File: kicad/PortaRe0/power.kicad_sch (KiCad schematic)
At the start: 37 parts, among them SW1 SW_START, SW2 KillSW, U1 BQ25895RTWR, U2 TPS61023DRLR, U3 AP2112K-3.3TRG1

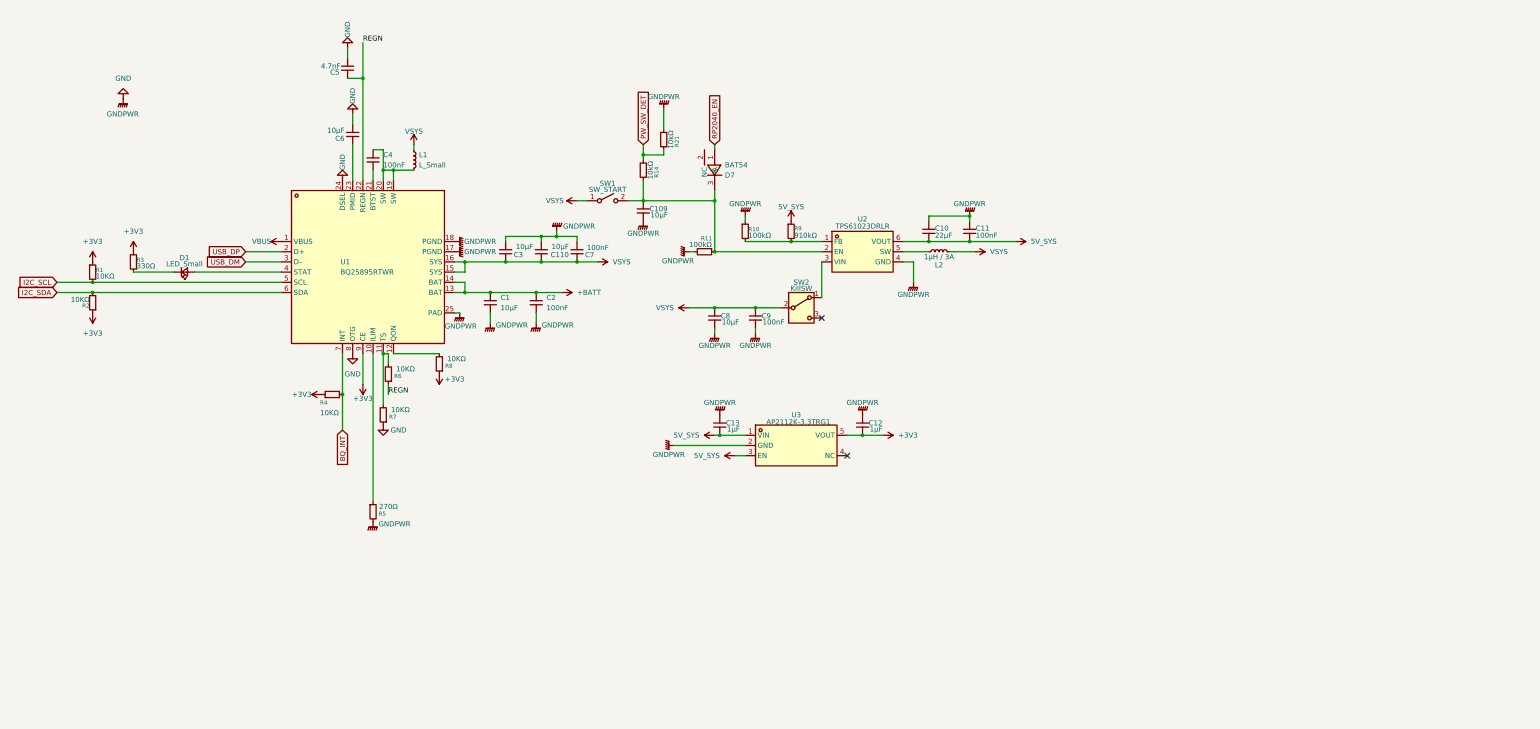
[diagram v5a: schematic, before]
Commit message: Docs: session18終了処理・PROGRESS/index更新・connectorsシート設計方針確定
- J_HDMI_CTRL: 24pin FPC 0.5mm (C2856805) ライブラリ取得・配置方針確定
- SBC接続: サブ基板→FPCに変更・スティフナーにMicro HDMIオス+USB-Cオス直付け方針
- connectors.kicad_sch 追加

Co-Authored-By: Claude Sonnet 4.6 <noreply@anthropic.com>
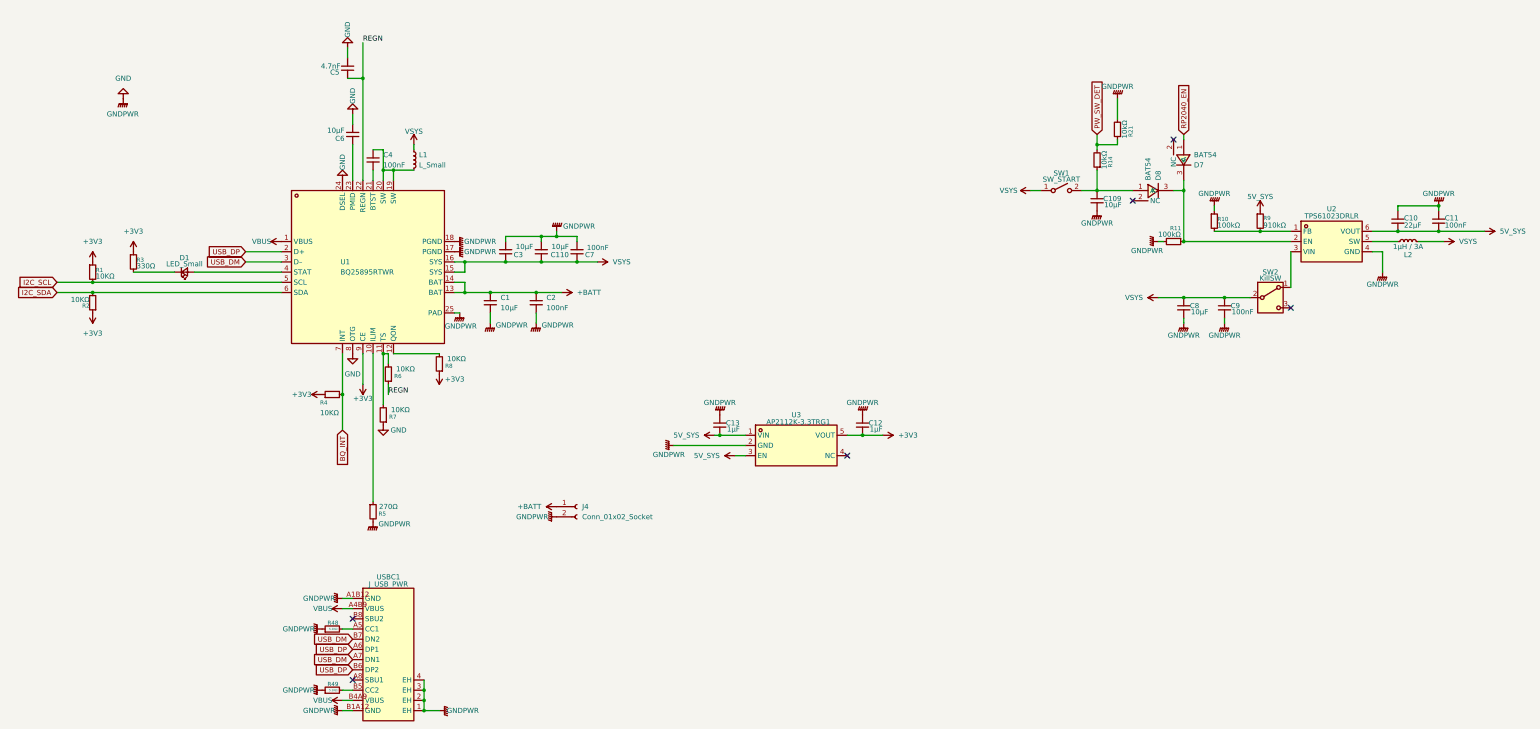
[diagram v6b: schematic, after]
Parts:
- added D8: BAT54, PortaRe0:SOT-23-3_L2.9-W1.4-P1.90-LS2.6-BR, symbol PortaRe0:BAT54_C466635
- added J4: Conn_01x02_Socket, symbol Connector:Conn_01x02_Socket
- added R48, R49: 5.1KΩ, symbol Device:R_Small
- added USBC1: J_USB_PWR, PortaRe0:USB-C_SMD-TYPE-C-31-M-12_1, symbol PortaRe0:TYPE-C-31-M-12
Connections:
- net +BATT: now also J4.1 (Pin_1)
- net GND: now also J4.2 (Pin_2), R48.1, R49.1, USBC1.1 (EH), USBC1.2 (EH), USBC1.3 (EH), USBC1.4 (EH), USBC1.A1B12 (GND), USBC1.B1A12 (GND)
- net USB_DM: now also USBC1.A7 (DN1), USBC1.B7 (DN2)
- net USB_DP: now also USBC1.A6 (DP1), USBC1.B6 (DP2)
- net VBUS: now also USBC1.A4B9 (VBUS), USBC1.B4A9 (VBUS)
- net at D7.3 (K), R11.1, U2.2 (EN): now also D8.3 (K); no longer C109.1, R14.1, SW1.2 (B)
- new net: R48.2, USBC1.A5 (CC1)
- new net: R49.2, USBC1.B5 (CC2)
- new net: C109.1, D8.1 (A), R14.1, SW1.2 (B)
- no-connect marks 2 -> 6
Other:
- moved on the sheet: C10, C109, C11, C8, C9, D7, L2, R10, R11, R14, R21, R9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

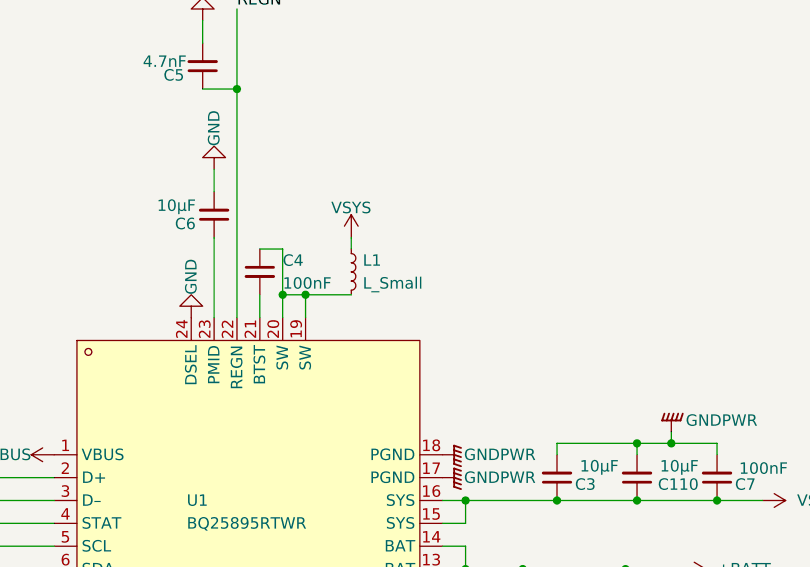
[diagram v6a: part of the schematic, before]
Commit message: KiCad/Docs: powerシートL1値2.2μH更新・README全面更新
- power.kicad_sch: L1インダクタ値を2.2μHに更新（BQ25895 TI例参照）
- README: バッテリー型番/容量修正・全シート完成状態に更新・部品C番号一覧追記

Co-Authored-By: Claude Sonnet 4.6 <noreply@anthropic.com>
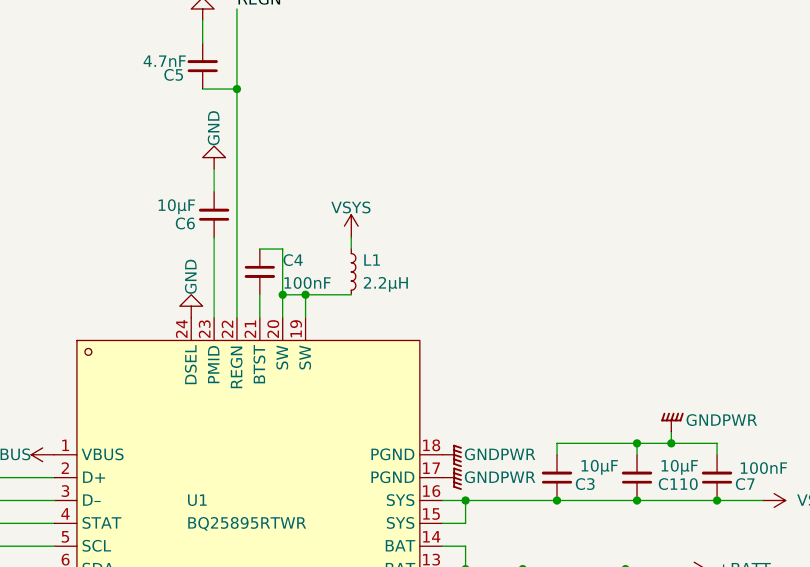
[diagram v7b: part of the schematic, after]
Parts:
- L1: value L_Small -> 2.2μH
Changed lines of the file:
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@@
 			)
 		)
-		(property "Value" "L_Small"
+		(property "Value" "2.2μH"
 			(at 113.03 52.0699 0)
 			(effects

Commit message: Docs/KiCad: session24終了処理・チェックシート作成・回路修正
- Claude/checklists/ 新規作成（IC設計レビュー用 01〜10）
- BQ25895修正: C5(4.7nF→4.7µF) / CE(3V3→GND) / QON(GND→NC)
- TPS61023修正: R_TOP(910kΩ→750kΩ, 5.1V) / SW2をVSYS直列に変更 / usb_hub SW4削除
- AP2112K: バイパスキャップ1µF→10µF
- PROGRESS.md・index.md更新

Co-Authored-By: Claude Sonnet 4.6 <noreply@anthropic.com>
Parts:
- removed R8: 10KΩ, symbol Device:R_Small
- added C113: 10μF, symbol Device:C_Small
- added C114: 100nF, symbol Device:C_Small
- C12, C13: value 1µF -> 10µF
- C5: value 4.7nF -> 4.7μF
- R9: value 910kΩ -> 750kΩ
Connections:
- net +3V3: no longer U1.9 (CE)
- net GND: now also U1.9 (CE), C113.2, C114.2
- net VBUS: now also C113.1, C114.1
- net VSYS: now also SW2.1 (A), U2.3 (VIN); no longer C110.1, C3.1, C7.1, SW2.2 (B), U1.15 (SYS), U1.16 (SYS)
- net at R3.2: now also D1.2 (A); no longer D1.1 (K)
- net at U1.4 (STAT): now also D1.1 (K); no longer D1.2 (A)
- new net: C110.1, C3.1, C7.1, SW2.2 (B), U1.15 (SYS), U1.16 (SYS)
- no-connect marks 6 -> 8
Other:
- moved on the sheet: C8, C9, D1, SW2
